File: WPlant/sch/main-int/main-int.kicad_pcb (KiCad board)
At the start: 4 copper layers, 135 x 85 mm, 140 parts, among them J1 PROG/JTAG, J10 Ext, J11 HSensor, J12 HSensor, J13 HSensor, J14 HSensor, J15 HSensor, J16 HSensor, J17 HSensor, J18 WaterLevel, J5 220V, J6 Conn_01x08_Pin, J8 eInk-Buttons, J9 Leak, M1 Motor_DC, Q1 FDS9926A, Q2 FDS9926A, Q3 FDS9926A, Q4 FDS9926A, U1 SIWG917Y121MGABAR, U10 SP485EEN-L/TR, U11 TXU0102QDCURQ1, U12 CD74HCT4051M96, U13 CD74HCT4051M96, U14 SN74LVC1G14DBV, U3 AP64352SP-13, U4 AP64352SP-13, U5 TC4427AEOA713, U6 AP2204R-5.0, U7 74HC594, U8 NC7S02P5, U9 INA180A2, X1 SIT1552AI-JE-DCC-32.768D

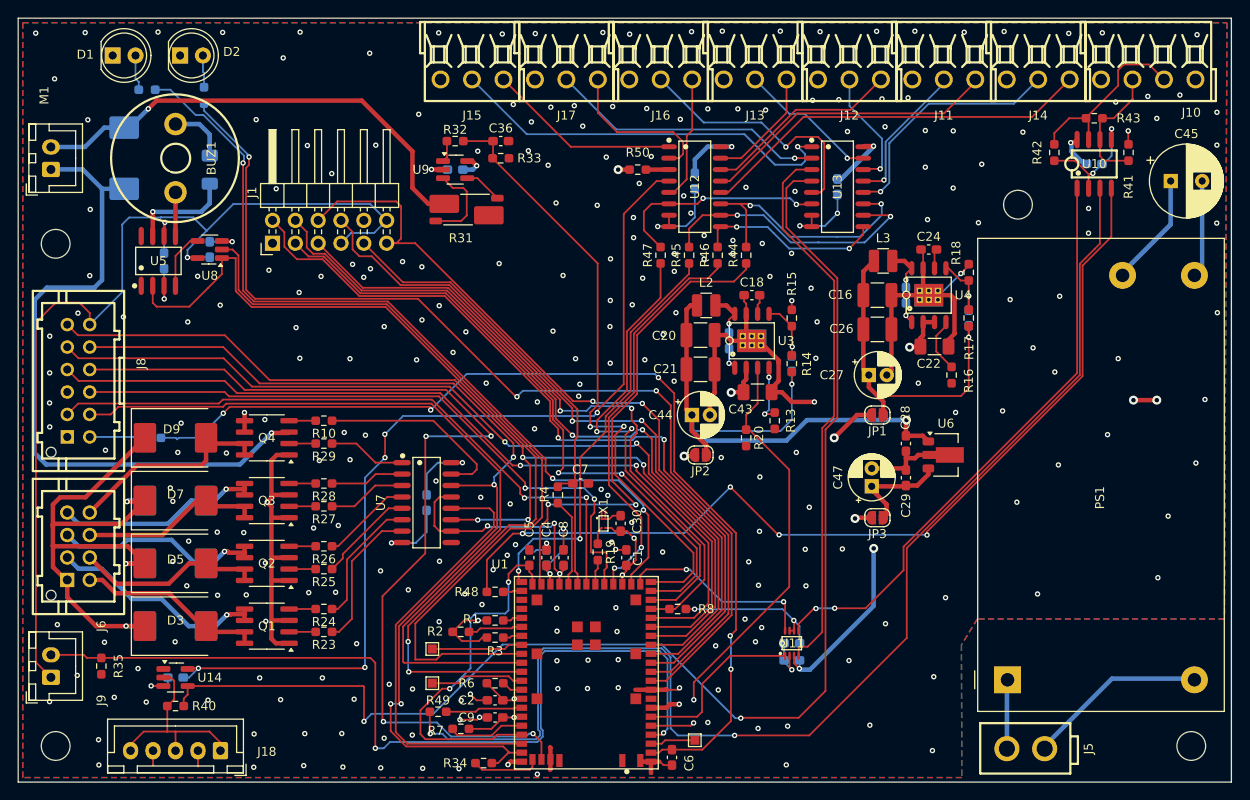
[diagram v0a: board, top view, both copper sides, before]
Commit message: Route of MainExt PCB done
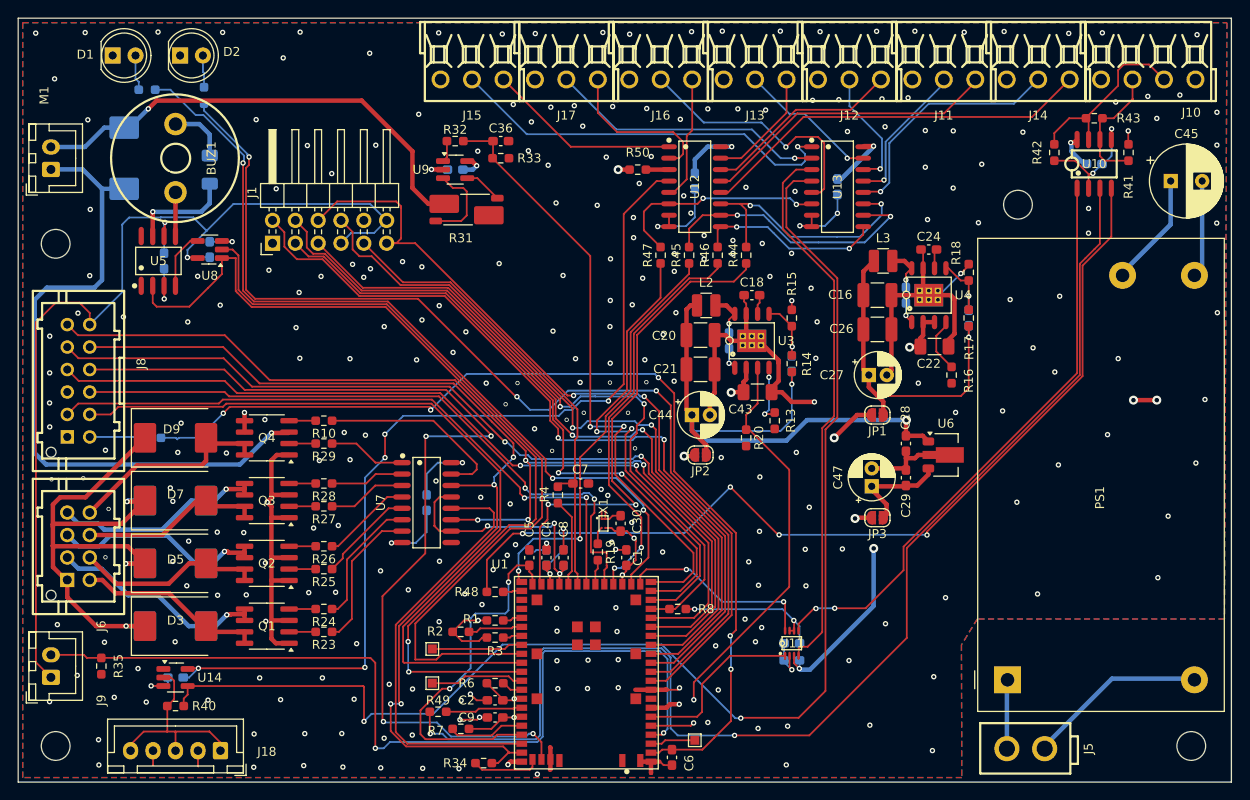
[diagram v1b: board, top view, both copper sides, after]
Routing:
- net PROG-RX: track 73.9 -> 76.0 mm
- net JTAG-TCK: track 79.4 -> 80.8 mm
- net Net-(U1-GPIO_55): track 114.2 -> 115.4 mm
- net JTAG-TDO: track 89.1 -> 89.9 mm
- net Net-(U1-ULP_GPIO_6): track 69.4 -> 68.8 mm
- net /~{eInkReset}: track 98.4 -> 97.8 mm
- net Net-(D8-A): track 23.1 -> 23.7 mm
- net GND: vias 286 -> 298

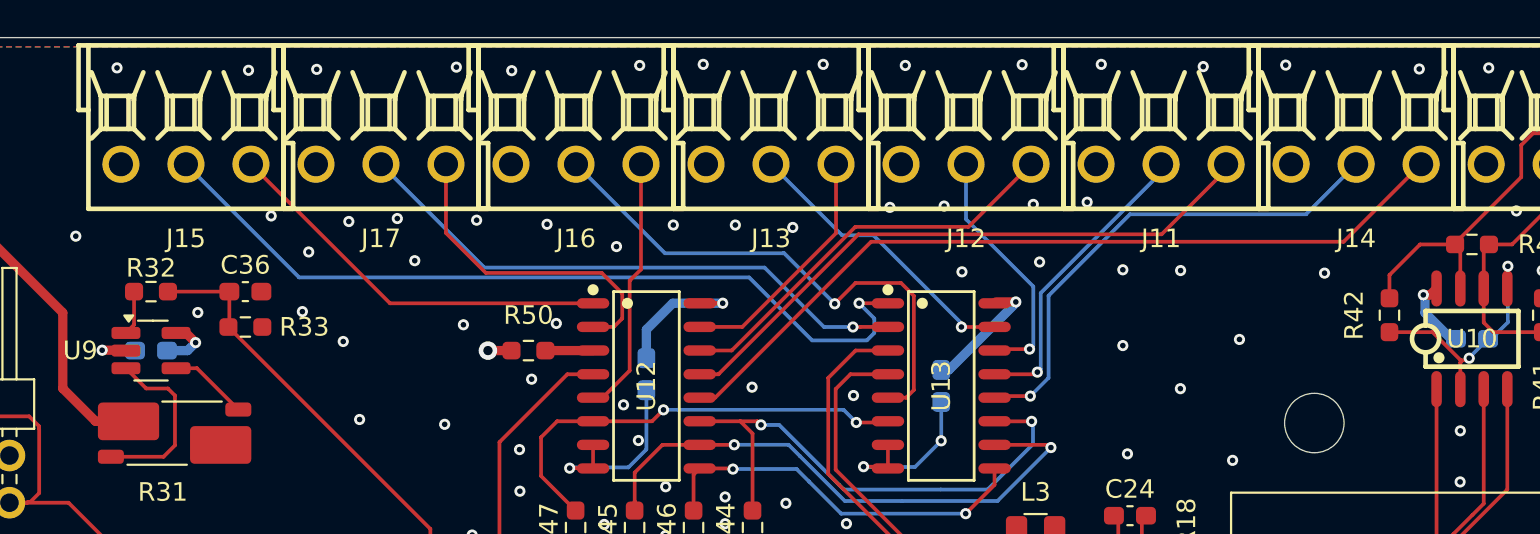
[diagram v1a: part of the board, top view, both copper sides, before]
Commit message: Route of WP project done
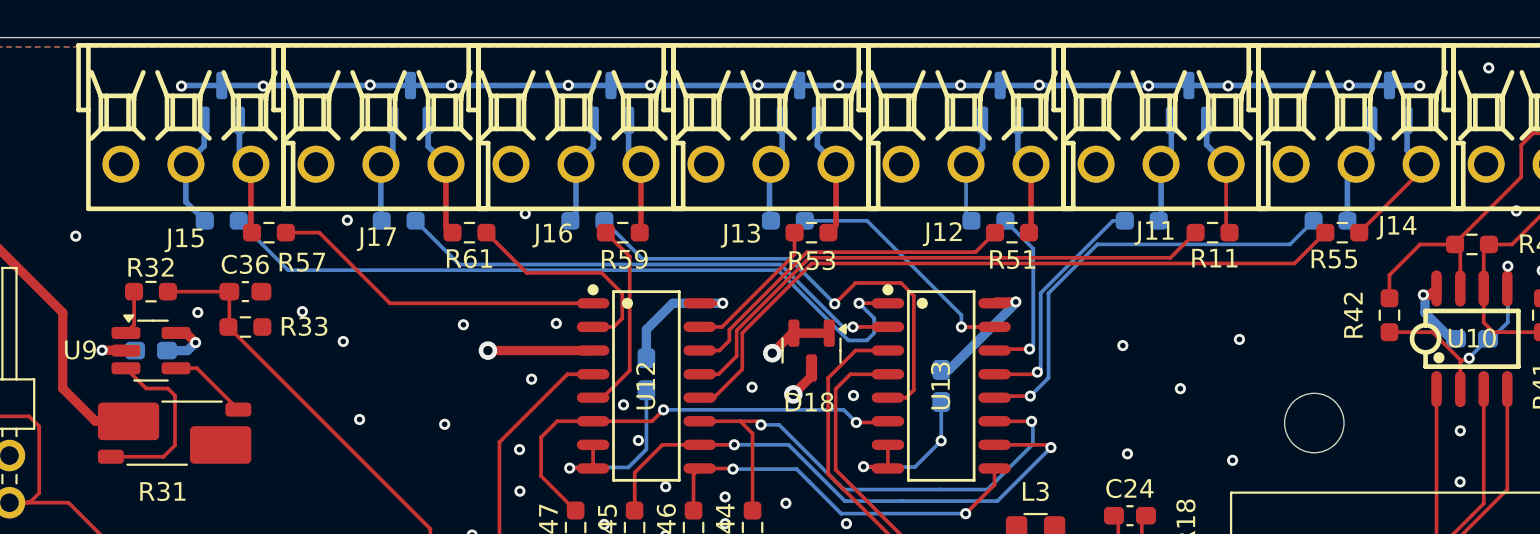
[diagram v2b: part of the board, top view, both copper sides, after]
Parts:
- added D11: MMBZ5V6, Package_TO_SOT_SMD:SOT-23, B.Cu at (190.5, 56.5)
- added D12: MMBZ5V6, Package_TO_SOT_SMD:SOT-23, B.Cu at (180.3, 56.5)
- added D13: MMBZ5V6, Package_TO_SOT_SMD:SOT-23, B.Cu at (169.5, 56.5)
- added D14: MMBZ5V6, Package_TO_SOT_SMD:SOT-23, B.Cu at (201.3, 56.5)
- added D15: MMBZ5V6, Package_TO_SOT_SMD:SOT-23, B.Cu at (138.4, 56.5)
- added D16: MMBZ5V6, Package_TO_SOT_SMD:SOT-23, B.Cu at (159.4, 56.5)
- added D17: MMBZ5V6, Package_TO_SOT_SMD:SOT-23, B.Cu at (148.6, 56.5)
- added D18: MMBZ5V6, Package_TO_SOT_SMD:SOT-23, F.Cu at (170.2, 69.8)
- added R11: 100, Resistor_SMD:R_0603_1608Metric_Pad0.98x0.95mm_HandSolder, F.Cu at (191.8, 63.5)
- added R51: 100, Resistor_SMD:R_0603_1608Metric_Pad0.98x0.95mm_HandSolder, F.Cu at (181.0, 63.5)
- added R52: 100, Resistor_SMD:R_0603_1608Metric_Pad0.98x0.95mm_HandSolder, B.Cu at (179.7, 62.9)
- added R53: 100, Resistor_SMD:R_0603_1608Metric_Pad0.98x0.95mm_HandSolder, F.Cu at (170.2, 63.5)
- added R54: 100, Resistor_SMD:R_0603_1608Metric_Pad0.98x0.95mm_HandSolder, B.Cu at (168.9, 62.9)
- added R55: 100, Resistor_SMD:R_0603_1608Metric_Pad0.98x0.95mm_HandSolder, F.Cu at (198.8, 63.5)
- added R56: 100, Resistor_SMD:R_0603_1608Metric_Pad0.98x0.95mm_HandSolder, B.Cu at (198.1, 62.9)
- added R57: 100, Resistor_SMD:R_0603_1608Metric_Pad0.98x0.95mm_HandSolder, F.Cu at (141.0, 63.5)
- added R58: 100, Resistor_SMD:R_0603_1608Metric_Pad0.98x0.95mm_HandSolder, B.Cu at (138.4, 62.9)
- added R59: 100, Resistor_SMD:R_0603_1608Metric_Pad0.98x0.95mm_HandSolder, F.Cu at (160.0, 63.5)
- added R60: 100, Resistor_SMD:R_0603_1608Metric_Pad0.98x0.95mm_HandSolder, B.Cu at (158.1, 62.9)
- added R61: 100, Resistor_SMD:R_0603_1608Metric_Pad0.98x0.95mm_HandSolder, F.Cu at (151.8, 63.5)
- added R62: 100, Resistor_SMD:R_0603_1608Metric_Pad0.98x0.95mm_HandSolder, B.Cu at (148.0, 62.9)
- R50: moved to B.Cu
- moved R50 33.8 mm to (188.0, 62.9)
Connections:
- J11 pad 1: /Humidity/P1 -> Net-(J11-Pin_1)
- J11 pad 2: /Humidity/F1 -> Net-(J11-Pin_2)
- J12 pad 1: /Humidity/P2 -> Net-(J12-Pin_1)
- J12 pad 2: /Humidity/F2 -> Net-(J12-Pin_2)
- J13 pad 1: /Humidity/P3 -> Net-(J13-Pin_1)
- J13 pad 2: /Humidity/F3 -> Net-(J13-Pin_2)
- J14 pad 1: /Humidity/P4 -> Net-(J14-Pin_1)
- J14 pad 2: /Humidity/F4 -> Net-(J14-Pin_2)
- J15 pad 1: /Humidity/P5 -> Net-(J15-Pin_1)
- J15 pad 2: /Humidity/F5 -> Net-(J15-Pin_2)
- J16 pad 1: /Humidity/P6 -> Net-(J16-Pin_1)
- J16 pad 2: /Humidity/F6 -> Net-(J16-Pin_2)
- J17 pad 1: /Humidity/P7 -> Net-(J17-Pin_1)
- J17 pad 2: /Humidity/F7 -> Net-(J17-Pin_2)
- R50 pad 1: +5V -> /Humidity/F1
- R50 pad 2: Net-(U12-A) -> Net-(J11-Pin_2)
- U12 pad 3: Net-(U12-A) -> +5V
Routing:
- net GND: track 223.1 -> 291.7 mm, vias 298 -> 281
- net +5V: track 203.4 -> 211.3 mm, vias 9 -> 10
- net Net-(J14-Pin_1): track 0.00 -> 7.74 mm
- net Net-(J13-Pin_1): track 0.00 -> 6.63 mm
- net Net-(J17-Pin_1): track 0.00 -> 6.59 mm
- net Net-(J11-Pin_1): track 0.00 -> 6.56 mm
- net Net-(J12-Pin_1): track 0.00 -> 6.39 mm
- net Net-(J16-Pin_1): track 0.00 -> 6.35 mm
- net Net-(J15-Pin_1): track 0.00 -> 6.33 mm
- net Net-(J15-Pin_2): track 0.00 -> 6.24 mm
- net Net-(J11-Pin_2): track 0.00 -> 6.19 mm
- net Net-(J14-Pin_2): track 0.00 -> 5.96 mm
- net Net-(J16-Pin_2): track 0.00 -> 5.92 mm
- net /Humidity/P7: track 17.6 -> 11.8 mm
- net Net-(J12-Pin_2): track 0.00 -> 5.70 mm
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
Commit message: Added connectors marks on back of PCBs
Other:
- board text added: "+"
- board text added: "-"
- board text added: "1"
- board text added: "2"
- board text added: "3"
- board text added: "4"
- board text added: "5"
- board text added: "6"
- board text added: "7"
- board text added: "A"
- board text added: "B"

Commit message: Update WP Sch (sheets titles, replaced wires by bus, update components values)
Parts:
- C30, C34, C35: value 0.1 -> 1.0
- C31: value 2.2 -> 10.0
- C36: value ? -> 2.2
- R21, R22: value 100K -> 510
- R32, R33: value R -> 10K
- R35: value ? -> 2M
- R40: value R -> 2M
- R44, R45, R46, R47, R48, R49: value R -> 1K
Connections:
- net Net-(U7-QA) renamed /Valves/Motor
- net Net-(U7-QB) renamed /Valves/V7
- net Net-(U7-QC) renamed /Valves/V6
- net Net-(U7-QD) renamed /Valves/V5
- net Net-(U7-QE) renamed /Valves/V4
- net Net-(U7-QF) renamed /Valves/V3
- net Net-(U7-QG) renamed /Valves/V2
- net Net-(U7-QH) renamed /Valves/V1
